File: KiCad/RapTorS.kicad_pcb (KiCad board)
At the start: 2 copper layers, 45 x 19 mm, 27 parts, among them IC1 EFM32HG308F64G-A-QFN24, J1 Molex 48037-2200, J2 TestPoint, J3 TestPoint, J4 TestPoint, J5 TestPoint, J6 TestPoint, U2 TLV71333PDBV, U3 E07-M1101S

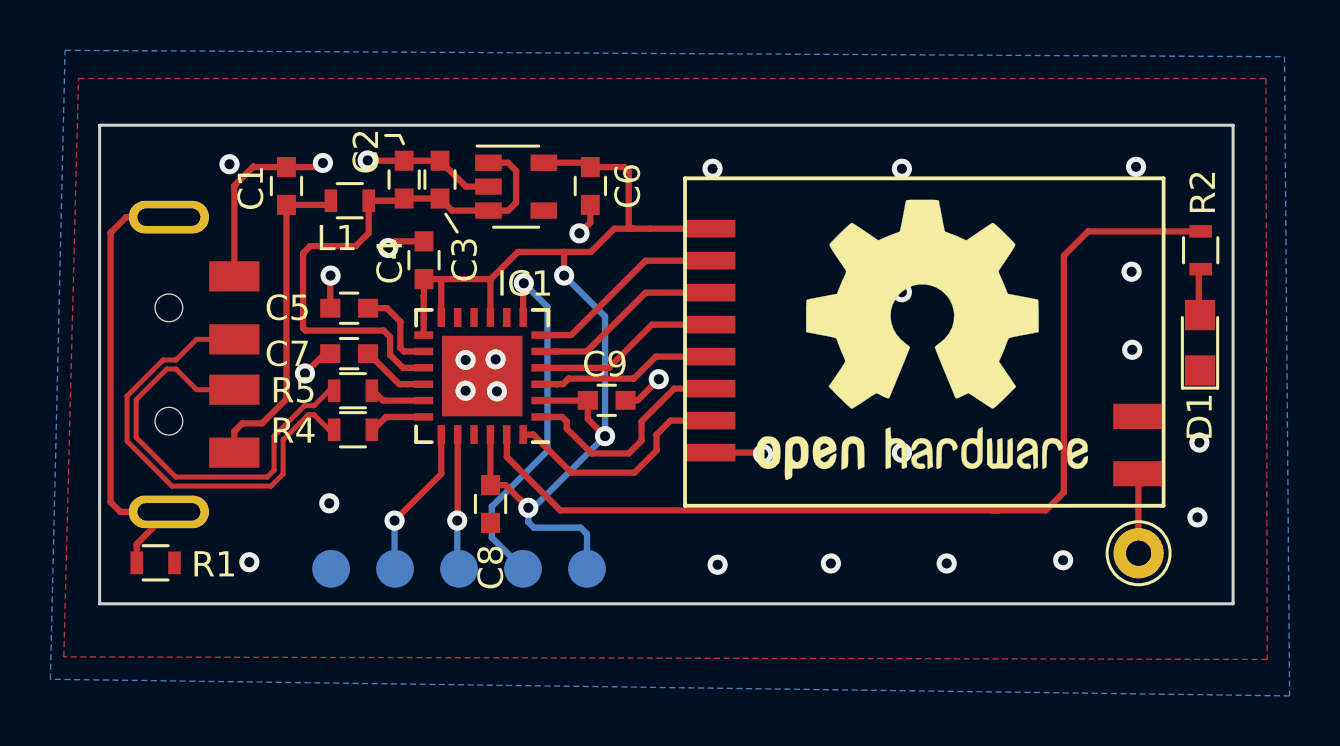
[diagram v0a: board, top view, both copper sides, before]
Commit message: correct pinout bug
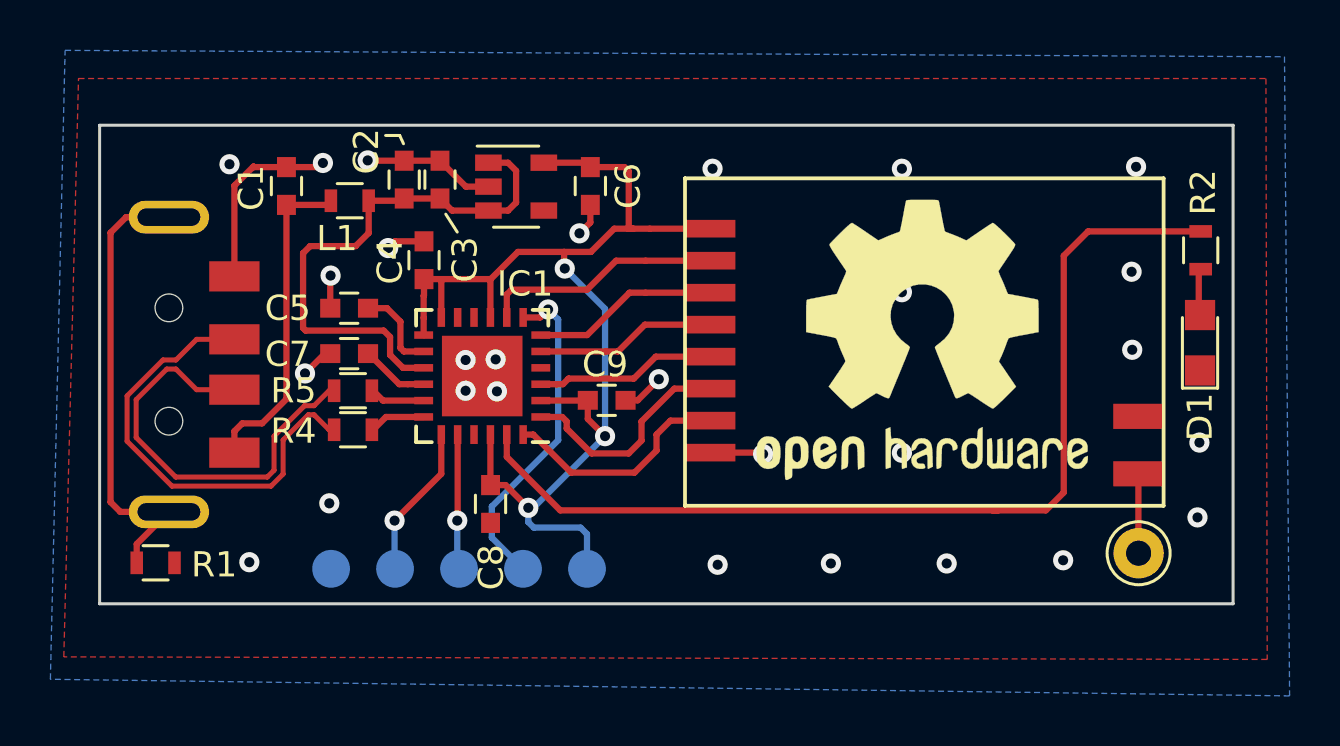
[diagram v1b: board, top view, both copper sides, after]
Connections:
- IC1 pad 4: SCK -> (no net)
- IC1 pad 5: CSN -> SCK
- IC1 pad 6: GDO0 -> CSN
- IC1 pad 8: (no net) -> GDO0
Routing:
- net GDO0: track 7.95 -> 9.54 mm
- net ~RESET: track 14.5 -> 13.2 mm
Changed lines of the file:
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@@
     (thickness 1.6)
     (drawings 20)
-    (tracks 244)
+    (tracks 250)
     (zones 0)
     (modules 27)
@@
     (34 B.Paste user)
     (35 F.Paste user)
-    (36 B.SilkS user)
-    (37 F.SilkS user)
+    (36 B.SilkS user hide)
+    (37 F.SilkS user hide)
     (38 B.Mask user)
     (39 F.Mask user)
@@
     (pad 3 smd rect (at -2.325 -0.325 180) (size 0.75 0.3) (layers F.Cu F.Paste F.Mask)
       (net 10 MOSI))
-    (pad 4 smd rect (at -2.325 0.325 180) (size 0.75 0.3) (layers F.Cu F.Paste F.Mask)
+    (pad 4 smd rect (at -2.325 0.325 180) (size 0.75 0.3) (layers F.Cu F.Paste F.Mask))
+    (pad 5 smd rect (at -2.325 0.975 180) (size 0.75 0.3) (layers F.Cu F.Paste F.Mask)
       (net 23 SCK))
-    (pad 5 smd rect (at -2.325 0.975 180) (size 0.75 0.3) (layers F.Cu F.Paste F.Mask)
+    (pad 6 smd rect (at -2.325 1.625 180) (size 0.75 0.3) (layers F.Cu F.Paste F.Mask)
       (net 13 CSN))
-    (pad 6 smd rect (at -2.325 1.625 180) (size 0.75 0.3) (layers F.Cu F.Paste F.Mask)
-      (net 11 GDO0))
     (pad 7 smd rect (at -1.625 2.325 270) (size 0.75 0.3) (layers F.Cu F.Paste F.Mask)
       (net 18 ~RESET))
-    (pad 8 smd rect (at -0.975 2.325 270) (size 0.75 0.3) (layers F.Cu F.Paste F.Mask))
+    (pad 8 smd rect (at -0.975 2.325 270) (size 0.75 0.3) (layers F.Cu F.Paste F.Mask)
+      (net 11 GDO0))
     (pad 9 smd rect (at -0.325 2.325 270) (size 0.75 0.3) (layers F.Cu F.Paste F.Mask)
       (net 1 +3V3))
@@
   (via (at 155.7782 106.3498) (size 0.8) (drill 0.4) (layers F.Cu B.Cu) (net 1))
   (segment (start 154.2796 105.4474) (end 154.8758 105.4474) (width 0.25) (layer F.Cu) (net 1))
-  (via (at 157.2006 97.1296) (size 0.8) (drill 0.4) (layers F.Cu B.Cu) (net 1))
-  (segment (start 157.2006 96.1898) (end 157.2006 97.1296) (width 0.25) (layer F.Cu) (net 1))
   (segment (start 155.3666 96.1898) (end 157.2006 96.1898) (width 0.25) (layer F.Cu) (net 1))
   (segment (start 157.2006 96.1898) (end 158.2674 96.1898) (width 0.25) (layer F.Cu) (net 1))
   (segment (start 158.8262 98.7552) (end 158.8262 103.505) (width 0.25) (layer B.Cu) (net 1))
-  (segment (start 157.2006 97.1296) (end 158.8262 98.7552) (width 0.25) (layer B.Cu) (net 1))
   (segment (start 155.9814 106.3498) (end 155.7782 106.3498) (width 0.25) (layer B.Cu) (net 1))
   (segment (start 158.8262 103.505) (end 155.9814 106.3498) (width 0.25) (layer B.Cu) (net 1))
@@
   (segment (start 155.7782 106.915485) (end 155.999915 107.1372) (width 0.25) (layer B.Cu) (net 1))
   (segment (start 155.7782 106.3498) (end 155.7782 106.915485) (width 0.25) (layer B.Cu) (net 1))
+  (via (at 157.226 96.8502) (size 0.8) (drill 0.4) (layers F.Cu B.Cu) (net 1))
+  (segment (start 157.2006 96.8248) (end 157.226 96.8502) (width 0.25) (layer F.Cu) (net 1))
+  (segment (start 157.2006 96.1898) (end 157.2006 96.8248) (width 0.25) (layer F.Cu) (net 1))
+  (segment (start 158.8262 98.4504) (end 158.8262 98.7552) (width 0.25) (layer B.Cu) (net 1))
+  (segment (start 157.226 96.8502) (end 158.8262 98.4504) (width 0.25) (layer B.Cu) (net 1))
   (segment (start 154.0908 92.5442) (end 154.1956 92.649) (width 0.25) (layer F.Cu) (net 2))
   (segment (start 154.9756 92.649) (end 155.2956 92.969) (width 0.25) (layer F.Cu) (net 2))
@@
   (segment (start 156.8994 101.4424) (end 156.9046 101.4476) (width 0.25) (layer F.Cu) (net 10))
   (segment (start 156.2744 101.4424) (end 156.8994 101.4424) (width 0.25) (layer F.Cu) (net 10))
+  (segment (start 162.3766 100.171) (end 163.0266 100.171) (width 0.25) (layer F.Cu) (net 10))
+  (segment (start 160.8394 100.3488) (end 163.0012 100.3488) (width 0.25) (layer F.Cu) (net 10))
+  (segment (start 159.9692 101.219) (end 160.8394 100.3488) (width 0.25) (layer F.Cu) (net 10))
   (segment (start 156.8994 101.4424) (end 157.155 101.4424) (width 0.25) (layer F.Cu) (net 10))
-  (segment (start 162.3766 100.171) (end 163.0266 100.171) (width 0.25) (layer F.Cu) (net 10))
   (segment (start 157.155 101.4424) (end 157.3784 101.219) (width 0.25) (layer F.Cu) (net 10))
   (segment (start 157.3784 101.219) (end 159.9692 101.219) (width 0.25) (layer F.Cu) (net 10))
-  (segment (start 160.8394 100.3488) (end 163.0012 100.3488) (width 0.25) (layer F.Cu) (net 10))
-  (segment (start 159.9692 101.219) (end 160.8394 100.3488) (width 0.25) (layer F.Cu) (net 10))
-  (segment (start 157.4794 99.4924) (end 160.433 96.5388) (width 0.25) (layer F.Cu) (net 11))
   (segment (start 160.433 96.5388) (end 163.0012 96.5388) (width 0.25) (layer F.Cu) (net 11))
-  (segment (start 156.2744 99.4924) (end 157.4794 99.4924) (width 0.25) (layer F.Cu) (net 11))
+  (segment (start 154.9244 98.7924) (end 154.9244 97.8818) (width 0.25) (layer F.Cu) (net 11))
+  (segment (start 154.9244 97.8818) (end 155.1178 97.6884) (width 0.25) (layer F.Cu) (net 11))
+  (segment (start 155.1178 97.6884) (end 158.115 97.6884) (width 0.25) (layer F.Cu) (net 11))
+  (segment (start 159.2646 96.5388) (end 160.433 96.5388) (width 0.25) (layer F.Cu) (net 11))
+  (segment (start 158.115 97.6884) (end 159.2646 96.5388) (width 0.25) (layer F.Cu) (net 11))
   (segment (start 155.5744 103.4424) (end 155.5744 103.6674) (width 0.25) (layer F.Cu) (net 12))
   (segment (start 161.4236 102.8888) (end 163.0012 102.8888) (width 0.25) (layer F.Cu) (net 12))
@@
   (segment (start 160.87 104.0774) (end 160.87 103.4424) (width 0.25) (layer F.Cu) (net 12))
   (segment (start 159.9946 104.9528) (end 160.87 104.0774) (width 0.25) (layer F.Cu) (net 12))
-  (segment (start 156.2744 100.1424) (end 156.8994 100.1424) (width 0.25) (layer F.Cu) (net 13))
   (segment (start 163.0012 97.8088) (end 160.433 97.8088) (width 0.25) (layer F.Cu) (net 13))
-  (segment (start 158.0994 100.1424) (end 156.8994 100.1424) (width 0.25) (layer F.Cu) (net 13))
-  (segment (start 160.433 97.8088) (end 158.0994 100.1424) (width 0.25) (layer F.Cu) (net 13))
+  (segment (start 156.2744 99.4924) (end 158.1144 99.4924) (width 0.25) (layer F.Cu) (net 13))
+  (segment (start 159.798 97.8088) (end 160.433 97.8088) (width 0.25) (layer F.Cu) (net 13))
+  (segment (start 158.1144 99.4924) (end 159.798 97.8088) (width 0.25) (layer F.Cu) (net 13))
   (segment (start 180.0012 108.1446) (end 180.0098 108.1532) (width 0.25) (layer F.Cu) (net 14))
   (segment (start 180.0012 104.9988) (end 180.0012 108.1446) (width 0.25) (layer F.Cu) (net 14))
@@
   (segment (start 160.274 103.6828) (end 160.274 102.9208) (width 0.25) (layer F.Cu) (net 17))
   (segment (start 159.766 104.1908) (end 160.274 103.6828) (width 0.25) (layer F.Cu) (net 17))
-  (via (at 155.6004 97.4344) (size 0.8) (drill 0.4) (layers F.Cu B.Cu) (net 18))
-  (segment (start 155.5744 97.4604) (end 155.6004 97.4344) (width 0.25) (layer F.Cu) (net 18))
-  (segment (start 155.5744 98.7924) (end 155.5744 97.4604) (width 0.25) (layer F.Cu) (net 18))
-  (segment (start 155.5692 108.7714) (end 154.3304 107.5326) (width 0.25) (layer B.Cu) (net 18))
-  (segment (start 154.3304 107.5326) (end 154.3304 106.299) (width 0.25) (layer B.Cu) (net 18))
-  (segment (start 154.3304 106.299) (end 156.5402 104.0892) (width 0.25) (layer B.Cu) (net 18))
-  (segment (start 156.5402 98.3742) (end 155.6004 97.4344) (width 0.25) (layer B.Cu) (net 18))
-  (segment (start 156.5402 104.0892) (end 156.5402 98.3742) (width 0.25) (layer B.Cu) (net 18))
+  (via (at 156.5656 98.4758) (size 0.8) (drill 0.4) (layers F.Cu B.Cu) (net 18))
+  (segment (start 156.249 98.7924) (end 156.5656 98.4758) (width 0.25) (layer F.Cu) (net 18))
+  (segment (start 155.5744 98.7924) (end 156.249 98.7924) (width 0.25) (layer F.Cu) (net 18))
+  (segment (start 154.3304 106.299) (end 154.3304 107.5326) (width 0.25) (layer B.Cu) (net 18))
+  (segment (start 154.3304 107.5326) (end 155.5692 108.7714) (width 0.25) (layer B.Cu) (net 18))
+  (segment (start 156.965599 103.663801) (end 154.3304 106.299) (width 0.25) (layer B.Cu) (net 18))
+  (segment (start 156.965599 98.875799) (end 156.965599 103.663801) (width 0.25) (layer B.Cu) (net 18))
+  (segment (start 156.5656 98.4758) (end 156.965599 98.875799) (width 0.25) (layer B.Cu) (net 18))
   (segment (start 150.0102 102.0924) (end 149.6194 101.7016) (width 0.25) (layer F.Cu) (net 19))
   (segment (start 151.6244 102.0924) (end 150.0102 102.0924) (width 0.25) (layer F.Cu) (net 19))
@@
   (segment (start 152.9588 108.701) (end 153.0292 108.7714) (width 0.25) (layer B.Cu) (net 22))
   (segment (start 152.9588 106.8578) (end 152.9588 108.701) (width 0.25) (layer B.Cu) (net 22))
-  (segment (start 160.687 99.0788) (end 163.0012 99.0788) (width 0.25) (layer F.Cu) (net 23))
-  (segment (start 158.9734 100.7924) (end 160.687 99.0788) (width 0.25) (layer F.Cu) (net 23))
-  (segment (start 156.2744 100.7924) (end 158.9734 100.7924) (width 0.25) (layer F.Cu) (net 23))
+  (segment (start 158.8614 100.1424) (end 156.2744 100.1424) (width 0.25) (layer F.Cu) (net 23))
+  (segment (start 160.4076 99.0788) (end 159.344 100.1424) (width 0.25) (layer F.Cu) (net 23))
+  (segment (start 159.344 100.1424) (end 158.8614 100.1424) (width 0.25) (layer F.Cu) (net 23))
+  (segment (start 163.0012 99.0788) (end 160.4076 99.0788) (width 0.25) (layer F.Cu) (net 23))
   (zone (net 3) (net_name GND) (layer F.Cu) (hatch edge 0.508)
     (connect_pads (clearance 0.508))

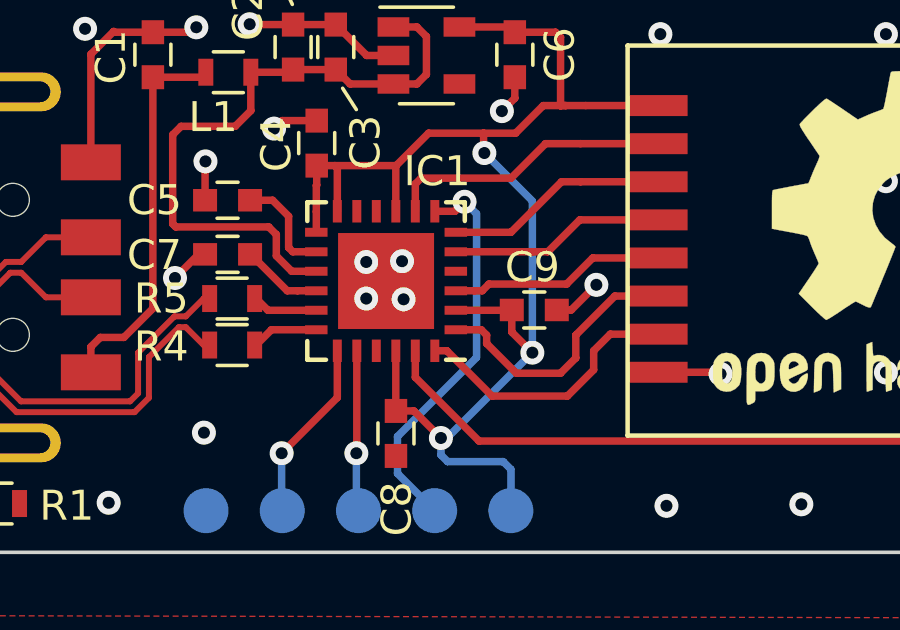
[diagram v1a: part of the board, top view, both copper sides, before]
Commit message: just move a via
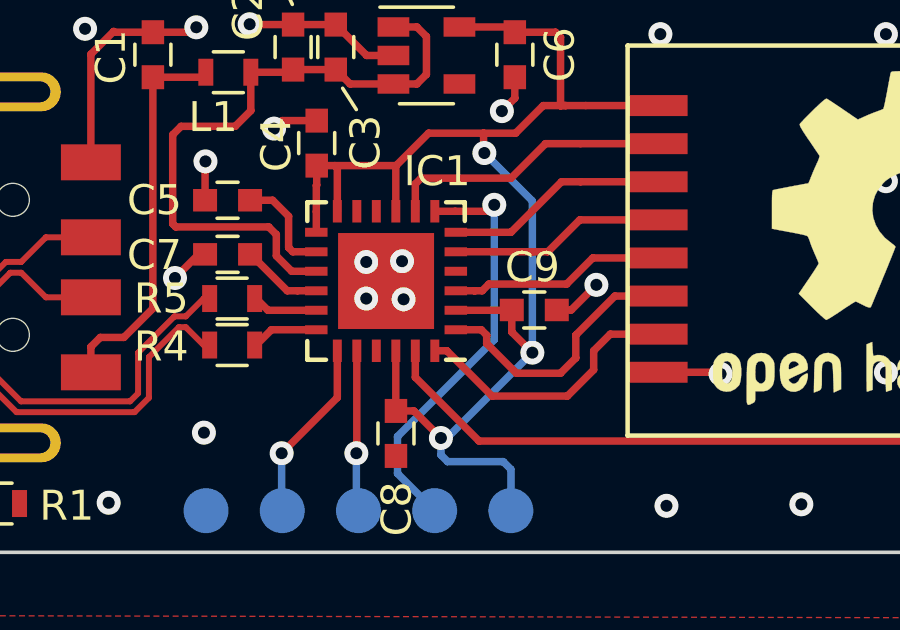
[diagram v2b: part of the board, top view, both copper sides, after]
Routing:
- net ~RESET: track 13.2 -> 14.1 mm
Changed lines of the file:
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@@
     (thickness 1.6)
     (drawings 20)
-    (tracks 250)
+    (tracks 251)
     (zones 0)
     (modules 27)
@@
   (segment (start 160.274 103.6828) (end 160.274 102.9208) (width 0.25) (layer F.Cu) (net 17))
   (segment (start 159.766 104.1908) (end 160.274 103.6828) (width 0.25) (layer F.Cu) (net 17))
-  (via (at 156.5656 98.4758) (size 0.8) (drill 0.4) (layers F.Cu B.Cu) (net 18))
-  (segment (start 156.249 98.7924) (end 156.5656 98.4758) (width 0.25) (layer F.Cu) (net 18))
   (segment (start 155.5744 98.7924) (end 156.249 98.7924) (width 0.25) (layer F.Cu) (net 18))
+  (segment (start 156.249 98.7924) (end 157.3158 98.7924) (width 0.25) (layer F.Cu) (net 18))
+  (via (at 157.5562 98.5774) (size 0.8) (drill 0.4) (layers F.Cu B.Cu) (net 18))
+  (segment (start 157.5308 98.5774) (end 157.5562 98.5774) (width 0.25) (layer F.Cu) (net 18))
+  (segment (start 157.3158 98.7924) (end 157.5308 98.5774) (width 0.25) (layer F.Cu) (net 18))
   (segment (start 154.3304 106.299) (end 154.3304 107.5326) (width 0.25) (layer B.Cu) (net 18))
   (segment (start 154.3304 107.5326) (end 155.5692 108.7714) (width 0.25) (layer B.Cu) (net 18))
-  (segment (start 156.965599 103.663801) (end 154.3304 106.299) (width 0.25) (layer B.Cu) (net 18))
-  (segment (start 156.965599 98.875799) (end 156.965599 103.663801) (width 0.25) (layer B.Cu) (net 18))
-  (segment (start 156.5656 98.4758) (end 156.965599 98.875799) (width 0.25) (layer B.Cu) (net 18))
+  (segment (start 157.5562 103.0732) (end 154.3304 106.299) (width 0.25) (layer B.Cu) (net 18))
+  (segment (start 157.5562 98.5774) (end 157.5562 103.0732) (width 0.25) (layer B.Cu) (net 18))
   (segment (start 150.0102 102.0924) (end 149.6194 101.7016) (width 0.25) (layer F.Cu) (net 19))
   (segment (start 151.6244 102.0924) (end 150.0102 102.0924) (width 0.25) (layer F.Cu) (net 19))

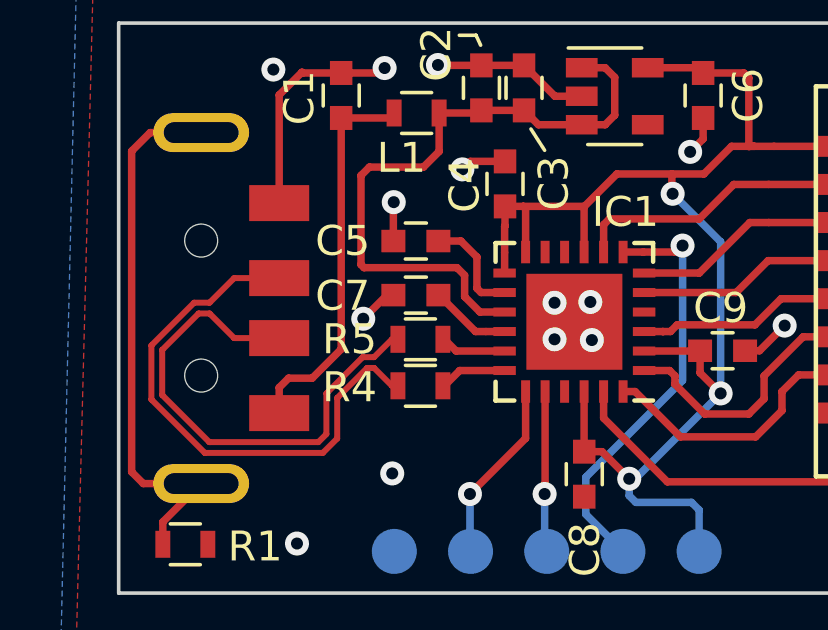
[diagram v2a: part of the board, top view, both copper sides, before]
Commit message: harmonize resistors and capacitors footprints due to KiCad issue #11
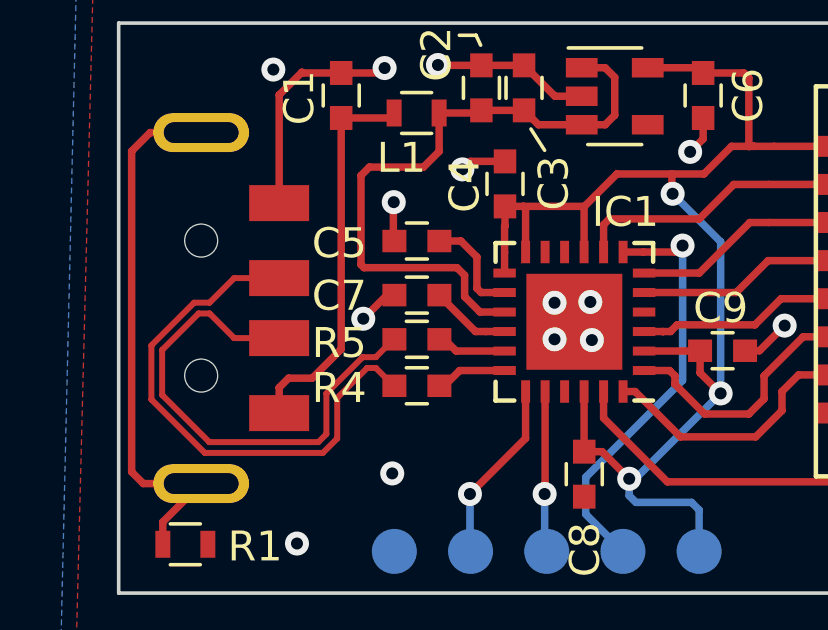
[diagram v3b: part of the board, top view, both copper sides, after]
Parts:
- R4, R5: footprint Resistors_SMD:R_0603 -> Capacitors_SMD:C_0603
- moved R4 0.12 mm to (148.7, 103.3)
- moved R5 0.12 mm to (148.7, 101.7)
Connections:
- IC1 pad 10: (no net) -> Net-(IC1-Pad10)
- IC1 pad 11: (no net) -> LED_DEBUG
- IC1 pad 21: (no net) -> Net-(IC1-Pad21)
- IC1 pad 4: (no net) -> Net-(IC1-Pad4)
- U2 pad 4: (no net) -> Net-(U2-Pad4)
